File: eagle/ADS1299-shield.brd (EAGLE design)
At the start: 101.6 x 53.3 mm, 133 parts, among them IC1 ADS1299IPAG, IC2 TPS72325DBVT, IC3 TPS73225DBVT, IC5 24AA256UID, IC6 TPS604XXDBV, IC7 OPA376DBV, IC8 OPA376DBV, IC9 TXS0102DCTR, J8 Electrode Connector, U2 TXB0108PWR, U3 TXB0108PWR

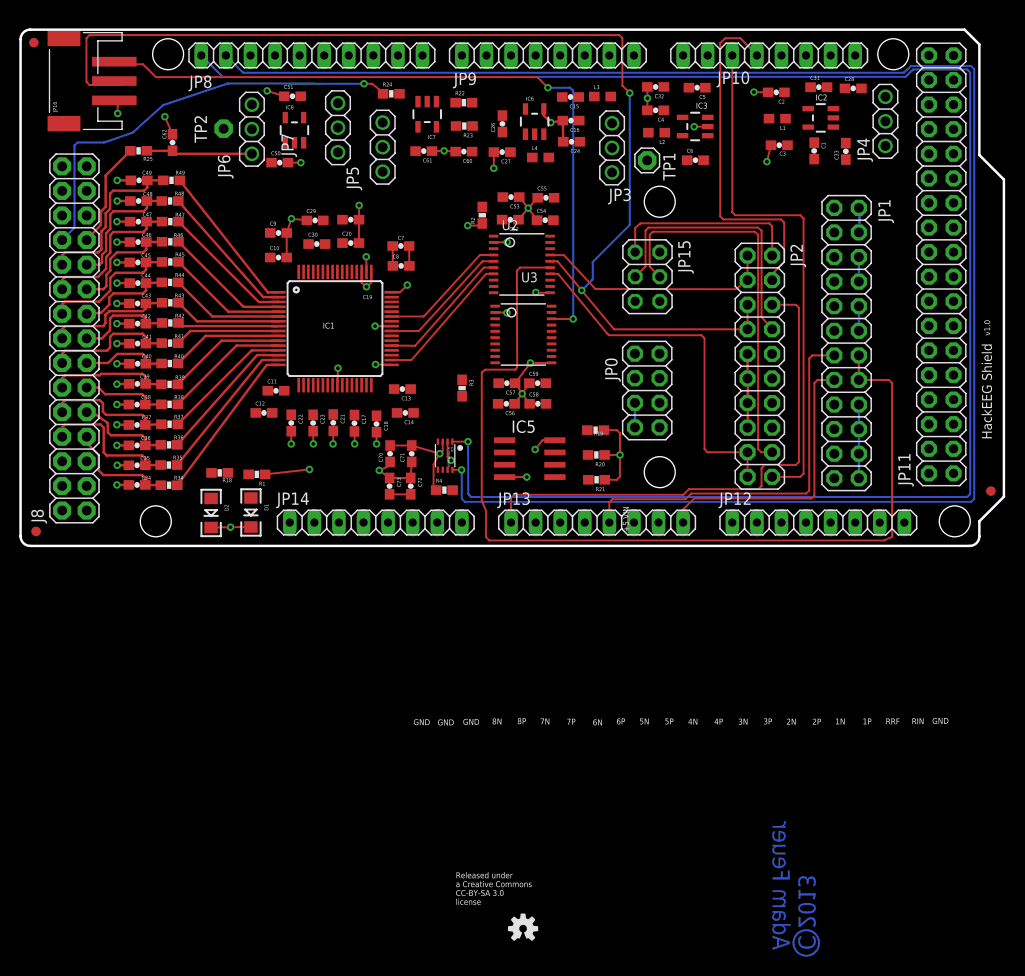
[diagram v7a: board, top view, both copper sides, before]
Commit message: partially routed some signals to avoid autorouter placing signals on DVDD layer - autorouter can route the board only using TOP and BOTTOM layers for signal traces
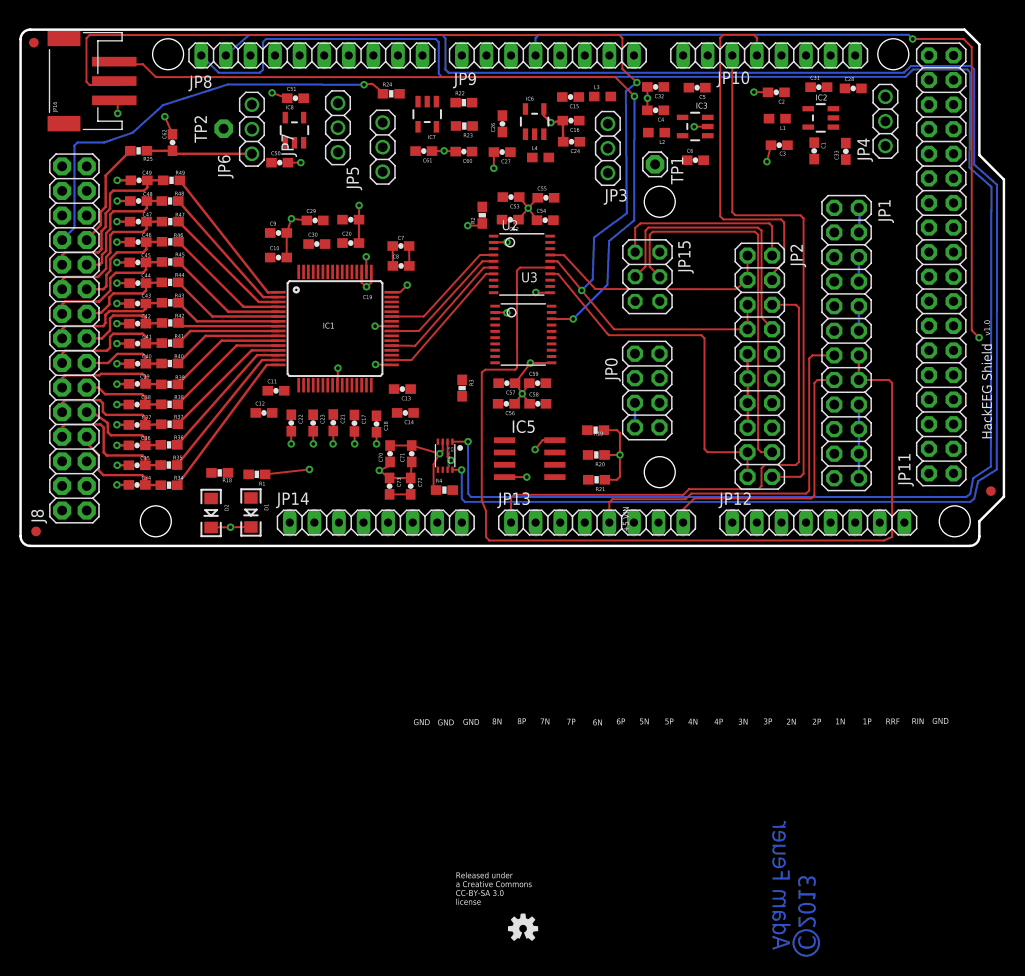
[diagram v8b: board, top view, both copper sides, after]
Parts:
- moved TP1 0.91 mm to (65.7, 39.5)
- moved JP3 0.43 mm to (60.8, 41.2)
- moved C51 0.37 mm to (28.5, 46.4)
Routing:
- net !ADC_CS_0: track 0.00 -> 78.9 mm, vias 0 -> 2
- net ADS_START: track 77.0 -> 85.7 mm
- net SCL1: track 183.5 -> 192.0 mm
- net SDA1: track 180.0 -> 185.7 mm
- net USART1_MISO: track 36.0 -> 37.6 mm
- net ADS_SPI_CLK: track 119.4 -> 120.4 mm
